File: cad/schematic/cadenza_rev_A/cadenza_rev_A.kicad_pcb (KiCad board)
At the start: 2 copper layers, 80 x 50 mm, 13 parts, among them J1 USB_B, U1 TLC5916, U10 HDSP-A151, U11 TLC5916, U12 HDSP-A151, U2 HDSP-A151, U3 TLC5916, U4 HDSP-A151, U5 TLC5916, U6 HDSP-A151, U7 TLC5916, U8 HDSP-A151, U9 TLC5916

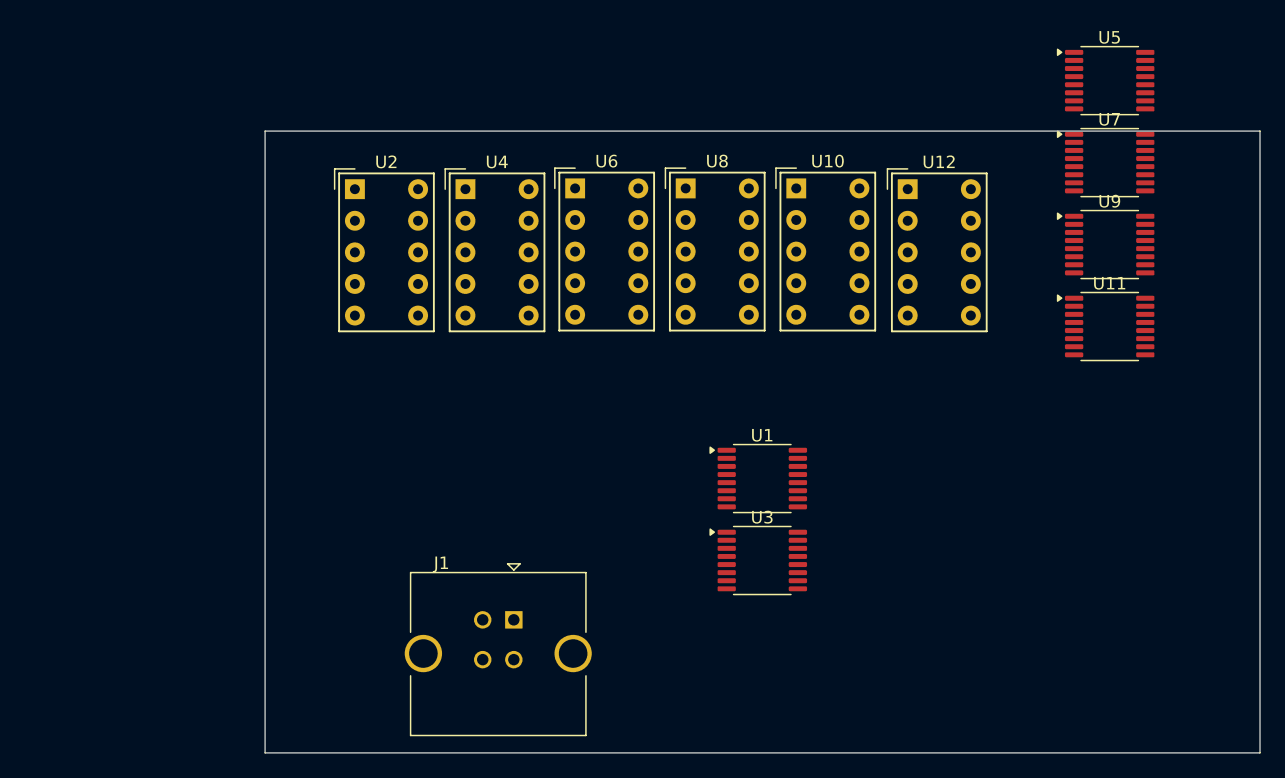
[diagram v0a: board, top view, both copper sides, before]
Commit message: added the MCU 7seg routing solution
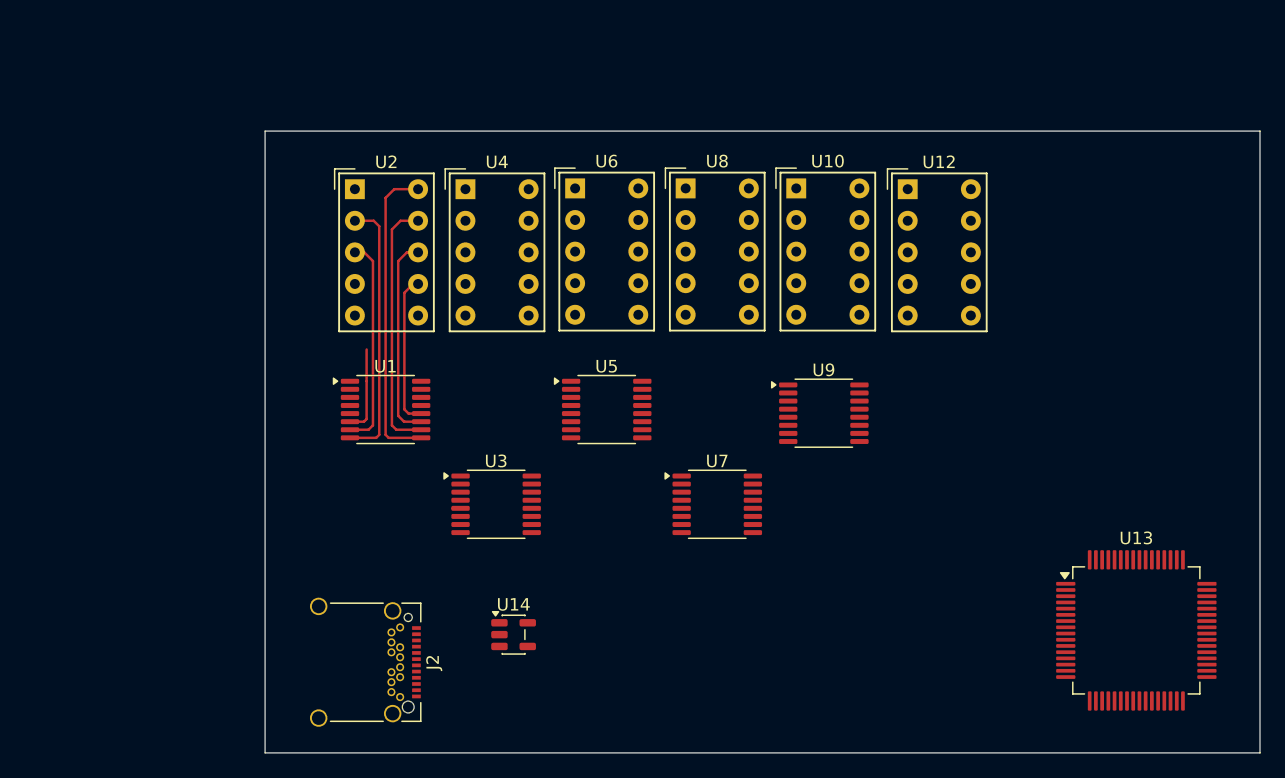
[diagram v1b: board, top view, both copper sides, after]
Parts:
- removed J1: USB_B, Connector_USB:USB_B_Amphenol_MUSB-D511_Vertical_Rugged
- removed U11: TLC5916, Package_SO:TSSOP-16_4.4x5mm_P0.65mm
- added J2: USB_C_Receptacle, Connector_USB:USB_C_Receptacle_Amphenol_12401548E4-2A_CircularHoles, F.Cu at (57.1, 92.7)
- added U13: STM32F105RCTx, Package_QFP:LQFP-64_10x10mm_P0.5mm, F.Cu at (120.1, 90.2)
- added U14: INA193, Package_TO_SOT_SMD:SOT-23-5, F.Cu at (70.0, 90.5)
- moved U5 48.3 mm to (77.5, 72.4)
- moved U7 41.8 mm to (86.4, 80.0)
- moved U1 30.8 mm to (59.7, 72.4)
- moved U9 26.7 mm to (94.9, 72.7)
- moved U3 21.9 mm to (68.6, 80.0)
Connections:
- U1 pad 1: unconnected-(U1-GND-Pad1) -> GND
- U1 pad 5: Net-(U1-~{OUT0}) -> unconnected-(U1-~{OUT0}-Pad5)
- U12 pad 10: Net-(U11-~{OUT0}) -> unconnected-(U12-A-Pad10)
- U12 pad 2: Net-(U11-~{OUT5}) -> unconnected-(U12-F-Pad2)
- U12 pad 3: Net-(U11-~{OUT6}) -> unconnected-(U12-G-Pad3)
- U12 pad 4: Net-(U11-~{OUT4}) -> unconnected-(U12-E-Pad4)
- U12 pad 5: Net-(U11-~{OUT3}) -> unconnected-(U12-D-Pad5)
- U12 pad 7: Net-(U11-~{OUT7}) -> unconnected-(U12-DP-Pad7)
- U12 pad 8: Net-(U11-~{OUT2}) -> unconnected-(U12-C-Pad8)
- U12 pad 9: Net-(U11-~{OUT1}) -> unconnected-(U12-B-Pad9)
- U2 pad 10: Net-(U1-~{OUT0}) -> Net-(U1-~{OUT4})
- U2 pad 2: Net-(U1-~{OUT5}) -> Net-(U1-~{OUT3})
- U2 pad 3: Net-(U1-~{OUT6}) -> Net-(U1-~{OUT2})
- U2 pad 4: Net-(U1-~{OUT4}) -> Net-(U1-~{OUT1})
- U2 pad 5: Net-(U1-~{OUT3}) -> unconnected-(U2-D-Pad5)
- U2 pad 8: Net-(U1-~{OUT2}) -> Net-(U1-~{OUT6})
- U2 pad 9: Net-(U1-~{OUT1}) -> Net-(U1-~{OUT5})
- U3 pad 10: Net-(U3-~{OUT5}) -> unconnected-(U3-~{OUT5}-Pad10)
- U3 pad 11: Net-(U3-~{OUT6}) -> unconnected-(U3-~{OUT6}-Pad11)
- U3 pad 12: Net-(U3-~{OUT7}) -> unconnected-(U3-~{OUT7}-Pad12)
- U3 pad 9: Net-(U3-~{OUT4}) -> unconnected-(U3-~{OUT4}-Pad9)
- U4 pad 10: Net-(U3-~{OUT0}) -> unconnected-(U4-A-Pad10)
- U4 pad 2: Net-(U3-~{OUT5}) -> Net-(U3-~{OUT3})
- U4 pad 3: Net-(U3-~{OUT6}) -> Net-(U3-~{OUT2})
- U4 pad 4: Net-(U3-~{OUT4}) -> Net-(U3-~{OUT1})
- U4 pad 5: Net-(U3-~{OUT3}) -> Net-(U3-~{OUT0})
- U4 pad 7: Net-(U3-~{OUT7}) -> unconnected-(U4-DP-Pad7)
- U4 pad 8: Net-(U3-~{OUT2}) -> unconnected-(U4-C-Pad8)
- U4 pad 9: Net-(U3-~{OUT1}) -> unconnected-(U4-B-Pad9)
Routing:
- net Net-(U1-~{OUT4}): track 0.00 -> 24.9 mm
- net Net-(U1-~{OUT3}): track 0.00 -> 21.4 mm
- net Net-(U1-~{OUT5}): track 0.00 -> 20.6 mm
- net Net-(U1-~{OUT2}): track 0.00 -> 16.9 mm
- net Net-(U1-~{OUT6}): track 0.00 -> 16.4 mm
- net Net-(U1-~{OUT7}): track 0.00 -> 12.9 mm
- net Net-(U1-~{OUT1}): track 0.00 -> 7.01 mm
- net Net-(U3-~{OUT0}): track 0.00 -> 0.66 mm

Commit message: added missing parts added buzzer interface
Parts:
- added J3: Conn_01x02, Connector_PinHeader_2.54mm:PinHeader_1x02_P2.54mm_Vertical, F.Cu at (114.0, 67.9)
- added Q1: BC547, Package_TO_SOT_THT:TO-92L_HandSolder, F.Cu at (118.2, 69.1)
- added R1: R_US, Resistor_SMD:R_0805_2012Metric_Pad1.20x1.40mm_HandSolder, F.Cu at (102.0, 85.6)
- added R2: R_US, Resistor_SMD:R_0805_2012Metric_Pad1.20x1.40mm_HandSolder, F.Cu at (79.8, 86.9)
- added R3: R_US, Resistor_SMD:R_0805_2012Metric_Pad1.20x1.40mm_HandSolder, F.Cu at (86.9, 87.1)
- added R4: 100, Resistor_SMD:R_0805_2012Metric_Pad1.20x1.40mm_HandSolder, F.Cu at (118.6, 73.2)
- added U11: TLC5916, Package_SO:TSSOP-16_4.4x5mm_P0.65mm, F.Cu at (104.3, 80.8)
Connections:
- net Net-(J2-VBUS-PadA4) renamed +5V
- net Net-(U1-VDD) renamed +3.3V
- U1 pad 13: unconnected-(U1-~{OE}(ED2)-Pad13) -> Net-(U1-~{OE}(ED2))
- U1 pad 14: unconnected-(U1-SDO-Pad14) -> Net-(U1-SDO)
- U1 pad 15: unconnected-(U1-R-EXT-Pad15) -> Net-(U1-R-EXT)
- U1 pad 3: unconnected-(U1-CLK-Pad3) -> Net-(U1-CLK)
- U1 pad 4: unconnected-(U1-LE(ED1)-Pad4) -> Net-(U1-LE(ED1))
- U1 pad 5: unconnected-(U1-~{OUT0}-Pad5) -> Net-(U1-~{OUT0})
- U10 pad 1: Net-(U10-CA-Pad1) -> +5VL
- U10 pad 10: Net-(U10-A) -> unconnected-(U10-A-Pad10)
- U10 pad 2: Net-(U10-F) -> unconnected-(U10-F-Pad2)
- U10 pad 3: Net-(U10-G) -> unconnected-(U10-G-Pad3)
- U10 pad 4: Net-(U10-E) -> unconnected-(U10-E-Pad4)
- U10 pad 5: Net-(U10-D) -> unconnected-(U10-D-Pad5)
- U10 pad 6: Net-(U10-CA-Pad1) -> +5VL
- U10 pad 7: Net-(U10-DP) -> unconnected-(U10-DP-Pad7)
- U10 pad 8: Net-(U10-C) -> unconnected-(U10-C-Pad8)
- U10 pad 9: Net-(U10-B) -> unconnected-(U10-B-Pad9)
- U12 pad 1: Net-(U12-CA-Pad1) -> +5VL
- U12 pad 6: Net-(U12-CA-Pad1) -> +5VL
- U2 pad 1: Net-(U2-CA-Pad1) -> +5VL
- U2 pad 5: unconnected-(U2-D-Pad5) -> Net-(U1-~{OUT0})
- U2 pad 6: Net-(U2-CA-Pad1) -> +5VL
- U3 pad 1: unconnected-(U3-GND-Pad1) -> GND
- U3 pad 13: unconnected-(U3-~{OE}(ED2)-Pad13) -> Net-(U1-~{OE}(ED2))
- U3 pad 14: unconnected-(U3-SDO-Pad14) -> Net-(U3-SDO)
- U3 pad 15: unconnected-(U3-R-EXT-Pad15) -> Net-(U3-R-EXT)
- U3 pad 2: unconnected-(U3-SDI-Pad2) -> Net-(U1-SDO)
- U3 pad 3: unconnected-(U3-CLK-Pad3) -> Net-(U1-CLK)
- U3 pad 4: unconnected-(U3-LE(ED1)-Pad4) -> Net-(U1-LE(ED1))
- U3 pad 5: Net-(U3-~{OUT0}) -> unconnected-(U3-~{OUT0}-Pad5)
- U3 pad 6: Net-(U3-~{OUT1}) -> unconnected-(U3-~{OUT1}-Pad6)
- U3 pad 7: Net-(U3-~{OUT2}) -> unconnected-(U3-~{OUT2}-Pad7)
- U3 pad 8: Net-(U3-~{OUT3}) -> unconnected-(U3-~{OUT3}-Pad8)
- U4 pad 1: Net-(U4-CA-Pad1) -> +5VL
- U4 pad 2: Net-(U3-~{OUT3}) -> unconnected-(U4-F-Pad2)
- U4 pad 3: Net-(U3-~{OUT2}) -> unconnected-(U4-G-Pad3)
- U4 pad 4: Net-(U3-~{OUT1}) -> unconnected-(U4-E-Pad4)
- U4 pad 5: Net-(U3-~{OUT0}) -> unconnected-(U4-D-Pad5)
- U4 pad 6: Net-(U4-CA-Pad1) -> +5VL
- U5 pad 1: unconnected-(U5-GND-Pad1) -> GND
- U5 pad 10: Net-(U5-~{OUT5}) -> unconnected-(U5-~{OUT5}-Pad10)
- U5 pad 11: Net-(U5-~{OUT6}) -> unconnected-(U5-~{OUT6}-Pad11)
- U5 pad 12: Net-(U5-~{OUT7}) -> unconnected-(U5-~{OUT7}-Pad12)
- U5 pad 13: unconnected-(U5-~{OE}(ED2)-Pad13) -> Net-(U1-~{OE}(ED2))
- U5 pad 14: unconnected-(U5-SDO-Pad14) -> Net-(U5-SDO)
- U5 pad 2: unconnected-(U5-SDI-Pad2) -> Net-(U3-SDO)
- U5 pad 3: unconnected-(U5-CLK-Pad3) -> Net-(U1-CLK)
- U5 pad 4: unconnected-(U5-LE(ED1)-Pad4) -> Net-(U1-LE(ED1))
- U5 pad 5: Net-(U5-~{OUT0}) -> unconnected-(U5-~{OUT0}-Pad5)
- U5 pad 6: Net-(U5-~{OUT1}) -> unconnected-(U5-~{OUT1}-Pad6)
- U5 pad 7: Net-(U5-~{OUT2}) -> unconnected-(U5-~{OUT2}-Pad7)
- U5 pad 8: Net-(U5-~{OUT3}) -> unconnected-(U5-~{OUT3}-Pad8)
- U5 pad 9: Net-(U5-~{OUT4}) -> unconnected-(U5-~{OUT4}-Pad9)
- U6 pad 1: Net-(U6-CA-Pad1) -> +5VL
- U6 pad 10: Net-(U5-~{OUT0}) -> unconnected-(U6-A-Pad10)
- U6 pad 2: Net-(U5-~{OUT5}) -> unconnected-(U6-F-Pad2)
- U6 pad 3: Net-(U5-~{OUT6}) -> unconnected-(U6-G-Pad3)
- U6 pad 4: Net-(U5-~{OUT4}) -> unconnected-(U6-E-Pad4)
- U6 pad 5: Net-(U5-~{OUT3}) -> unconnected-(U6-D-Pad5)
- U6 pad 6: Net-(U6-CA-Pad1) -> +5VL
- U6 pad 7: Net-(U5-~{OUT7}) -> unconnected-(U6-DP-Pad7)
- U6 pad 8: Net-(U5-~{OUT2}) -> unconnected-(U6-C-Pad8)
- U6 pad 9: Net-(U5-~{OUT1}) -> unconnected-(U6-B-Pad9)
- U7 pad 1: unconnected-(U7-GND-Pad1) -> GND
- U7 pad 10: Net-(U7-~{OUT5}) -> unconnected-(U7-~{OUT5}-Pad10)
- U7 pad 11: Net-(U7-~{OUT6}) -> unconnected-(U7-~{OUT6}-Pad11)
- U7 pad 12: Net-(U7-~{OUT7}) -> unconnected-(U7-~{OUT7}-Pad12)
- U7 pad 13: unconnected-(U7-~{OE}(ED2)-Pad13) -> Net-(U1-~{OE}(ED2))
- U7 pad 14: unconnected-(U7-SDO-Pad14) -> Net-(U7-SDO)
- U7 pad 2: unconnected-(U7-SDI-Pad2) -> Net-(U5-SDO)
- U7 pad 3: unconnected-(U7-CLK-Pad3) -> Net-(U1-CLK)
- U7 pad 4: unconnected-(U7-LE(ED1)-Pad4) -> Net-(U1-LE(ED1))
- U7 pad 5: Net-(U7-~{OUT0}) -> unconnected-(U7-~{OUT0}-Pad5)
- U7 pad 6: Net-(U7-~{OUT1}) -> unconnected-(U7-~{OUT1}-Pad6)
- U7 pad 7: Net-(U7-~{OUT2}) -> unconnected-(U7-~{OUT2}-Pad7)
- U7 pad 8: Net-(U7-~{OUT3}) -> unconnected-(U7-~{OUT3}-Pad8)
- U7 pad 9: Net-(U7-~{OUT4}) -> unconnected-(U7-~{OUT4}-Pad9)
- U8 pad 1: Net-(U8-CA-Pad1) -> +5VL
- U8 pad 10: Net-(U7-~{OUT0}) -> unconnected-(U8-A-Pad10)
- U8 pad 2: Net-(U7-~{OUT5}) -> unconnected-(U8-F-Pad2)
- U8 pad 3: Net-(U7-~{OUT6}) -> unconnected-(U8-G-Pad3)
- U8 pad 4: Net-(U7-~{OUT4}) -> unconnected-(U8-E-Pad4)
- U8 pad 5: Net-(U7-~{OUT3}) -> unconnected-(U8-D-Pad5)
- U8 pad 6: Net-(U8-CA-Pad1) -> +5VL
- U8 pad 7: Net-(U7-~{OUT7}) -> unconnected-(U8-DP-Pad7)
- U8 pad 8: Net-(U7-~{OUT2}) -> unconnected-(U8-C-Pad8)
- U8 pad 9: Net-(U7-~{OUT1}) -> unconnected-(U8-B-Pad9)
- U9 pad 1: unconnected-(U9-GND-Pad1) -> GND
- U9 pad 10: Net-(U10-F) -> unconnected-(U9-~{OUT5}-Pad10)
- U9 pad 11: Net-(U10-G) -> unconnected-(U9-~{OUT6}-Pad11)
- U9 pad 12: Net-(U10-DP) -> unconnected-(U9-~{OUT7}-Pad12)
- U9 pad 13: unconnected-(U9-~{OE}(ED2)-Pad13) -> Net-(U1-~{OE}(ED2))
- U9 pad 14: unconnected-(U9-SDO-Pad14) -> Net-(U11-SDI)
- U9 pad 2: unconnected-(U9-SDI-Pad2) -> Net-(U7-SDO)
- U9 pad 3: unconnected-(U9-CLK-Pad3) -> Net-(U1-CLK)
- U9 pad 4: unconnected-(U9-LE(ED1)-Pad4) -> Net-(U1-LE(ED1))
- U9 pad 5: Net-(U10-A) -> unconnected-(U9-~{OUT0}-Pad5)
- U9 pad 6: Net-(U10-B) -> unconnected-(U9-~{OUT1}-Pad6)
- U9 pad 7: Net-(U10-C) -> unconnected-(U9-~{OUT2}-Pad7)
- U9 pad 8: Net-(U10-D) -> unconnected-(U9-~{OUT3}-Pad8)
- U9 pad 9: Net-(U10-E) -> unconnected-(U9-~{OUT4}-Pad9)
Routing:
- net Net-(U1-~{OUT0}): track 0.00 -> 11.1 mm
- net Net-(U1-~{OUT1}): track 7.01 -> 14.0 mm, vias 0 -> 1
- net unconnected-(U3-~{OUT0}-Pad5): track 0.00 -> 0.66 mm
- net Net-(U3-~{OUT0}): track 0.66 -> 0.00 mm

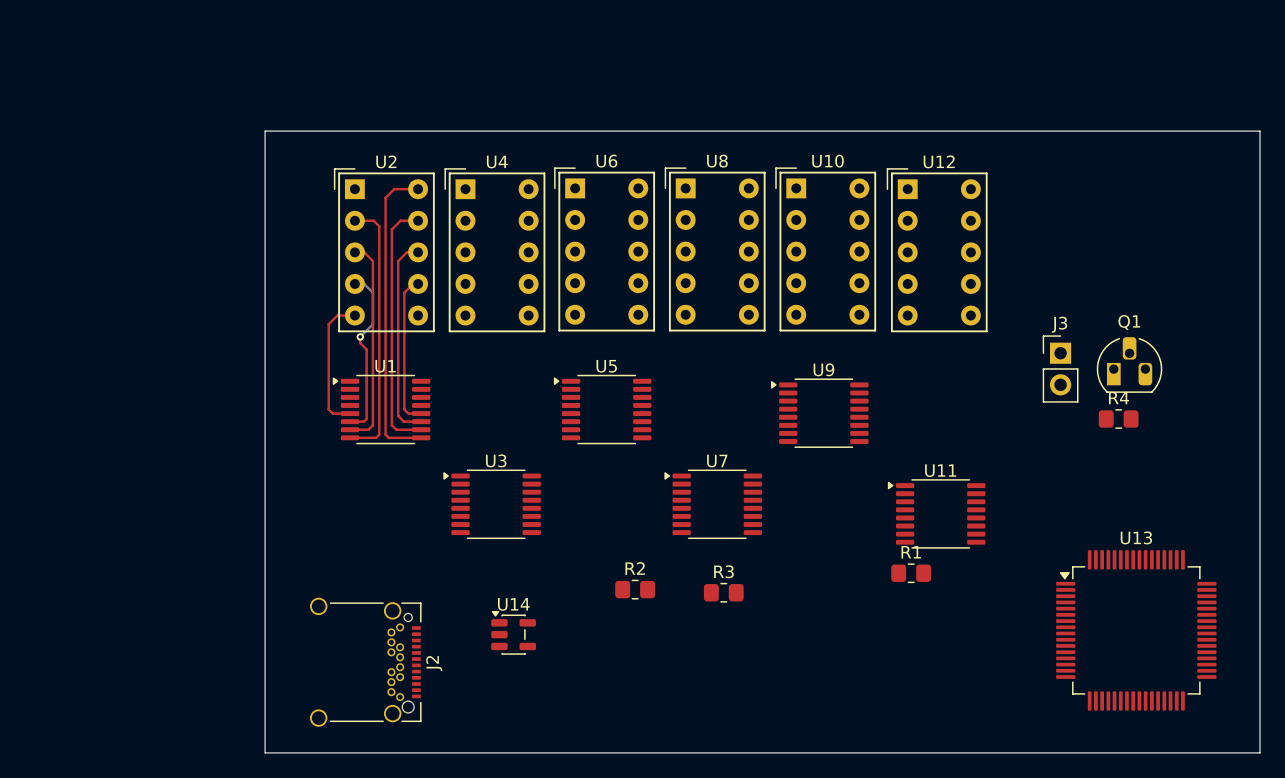
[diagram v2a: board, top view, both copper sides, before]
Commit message: added the LEDs to indicate the acceleration
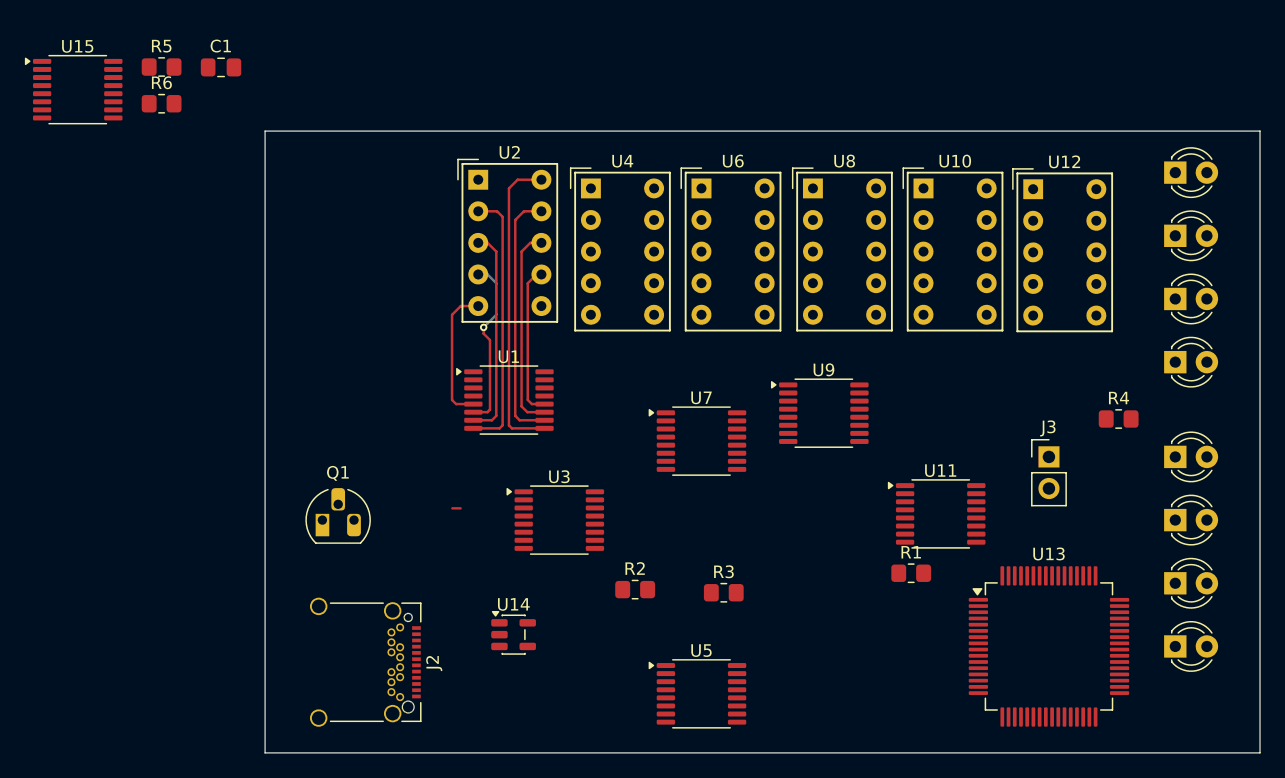
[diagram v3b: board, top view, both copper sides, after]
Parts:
- added C1: 100nF, Capacitor_SMD:C_0805_2012Metric_Pad1.18x1.45mm_HandSolder, F.Cu at (46.5, 44.9)
- added D1: LED, LED_THT:LED_D3.0mm, F.Cu at (123.2, 53.3)
- added D2: LED, LED_THT:LED_D3.0mm, F.Cu at (123.2, 58.4)
- added D3: LED, LED_THT:LED_D3.0mm, F.Cu at (123.2, 63.5)
- added D4: LED, LED_THT:LED_D3.0mm, F.Cu at (123.2, 68.6)
- added D5: LED, LED_THT:LED_D3.0mm, F.Cu at (123.2, 76.2)
- added D6: LED, LED_THT:LED_D3.0mm, F.Cu at (123.2, 81.3)
- added D7: LED, LED_THT:LED_D3.0mm, F.Cu at (123.2, 86.4)
- added D8: LED, LED_THT:LED_D3.0mm, F.Cu at (123.2, 91.4)
- added R5: R_US, Resistor_SMD:R_0805_2012Metric_Pad1.20x1.40mm_HandSolder, F.Cu at (41.7, 44.9)
- added R6: R_US, Resistor_SMD:R_0805_2012Metric_Pad1.20x1.40mm_HandSolder, F.Cu at (41.7, 47.8)
- added U15: TLC5916, Package_SO:TSSOP-16_4.4x5mm_P0.65mm, F.Cu at (34.9, 46.7)
- moved Q1 64.8 mm to (54.6, 81.3)
- moved U5 24.1 mm to (85.1, 95.2)
- moved U10 10.2 mm to (102.9, 54.6)
- moved U8 10.2 mm to (94.1, 54.6)
- moved U6 10.2 mm to (85.1, 54.6)
- moved U4 10.1 mm to (76.2, 54.6)
- moved U12 10.1 mm to (111.8, 54.7)
- moved U1 9.95 mm to (69.6, 71.6)
- moved U2 9.95 mm to (67.1, 53.9)
- moved J3 8.39 mm to (113.0, 76.2)
- moved U13 7.14 mm to (113.0, 91.4)
- moved U3 5.24 mm to (73.7, 81.3)
- moved U7 5.24 mm to (85.1, 74.9)
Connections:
- R3 pad 1: unconnected-(R3-Pad1) -> Net-(U5-R-EXT)
- U11 pad 14: unconnected-(U11-SDO-Pad14) -> Net-(U11-SDO)
- U13 pad 1: unconnected-(U13-VBAT-Pad1) -> +3.3V
- U13 pad 12: unconnected-(U13-VSSA-Pad12) -> GND
- U13 pad 13: unconnected-(U13-VDDA-Pad13) -> +3.3V
- U13 pad 18: Net-(U13-VSS-Pad18) -> GND
- U13 pad 19: unconnected-(U13-VDD-Pad19) -> +3.3V
- U13 pad 31: Net-(U13-VSS-Pad18) -> GND
- U13 pad 32: unconnected-(U13-VDD-Pad32) -> +3.3V
- U13 pad 47: Net-(U13-VSS-Pad18) -> GND
- U13 pad 48: unconnected-(U13-VDD-Pad48) -> +3.3V
- U13 pad 63: Net-(U13-VSS-Pad18) -> GND
- U13 pad 64: unconnected-(U13-VDD-Pad64) -> +3.3V
- U5 pad 15: unconnected-(U5-R-EXT-Pad15) -> Net-(U5-R-EXT)
